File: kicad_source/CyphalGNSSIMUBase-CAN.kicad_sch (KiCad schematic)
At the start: 47 parts, among them CN1 RASPBERRYPI_PICO, CN12 S3B-PH-SM4-TB, CN2 SM04B-SRSS-TB, CN3 SM04B-SRSS-TB, CN7 DNI, CN8 DNI, SW1 PTS636 SM43 SMTR LFS, U3 M24C64-RMN6TP

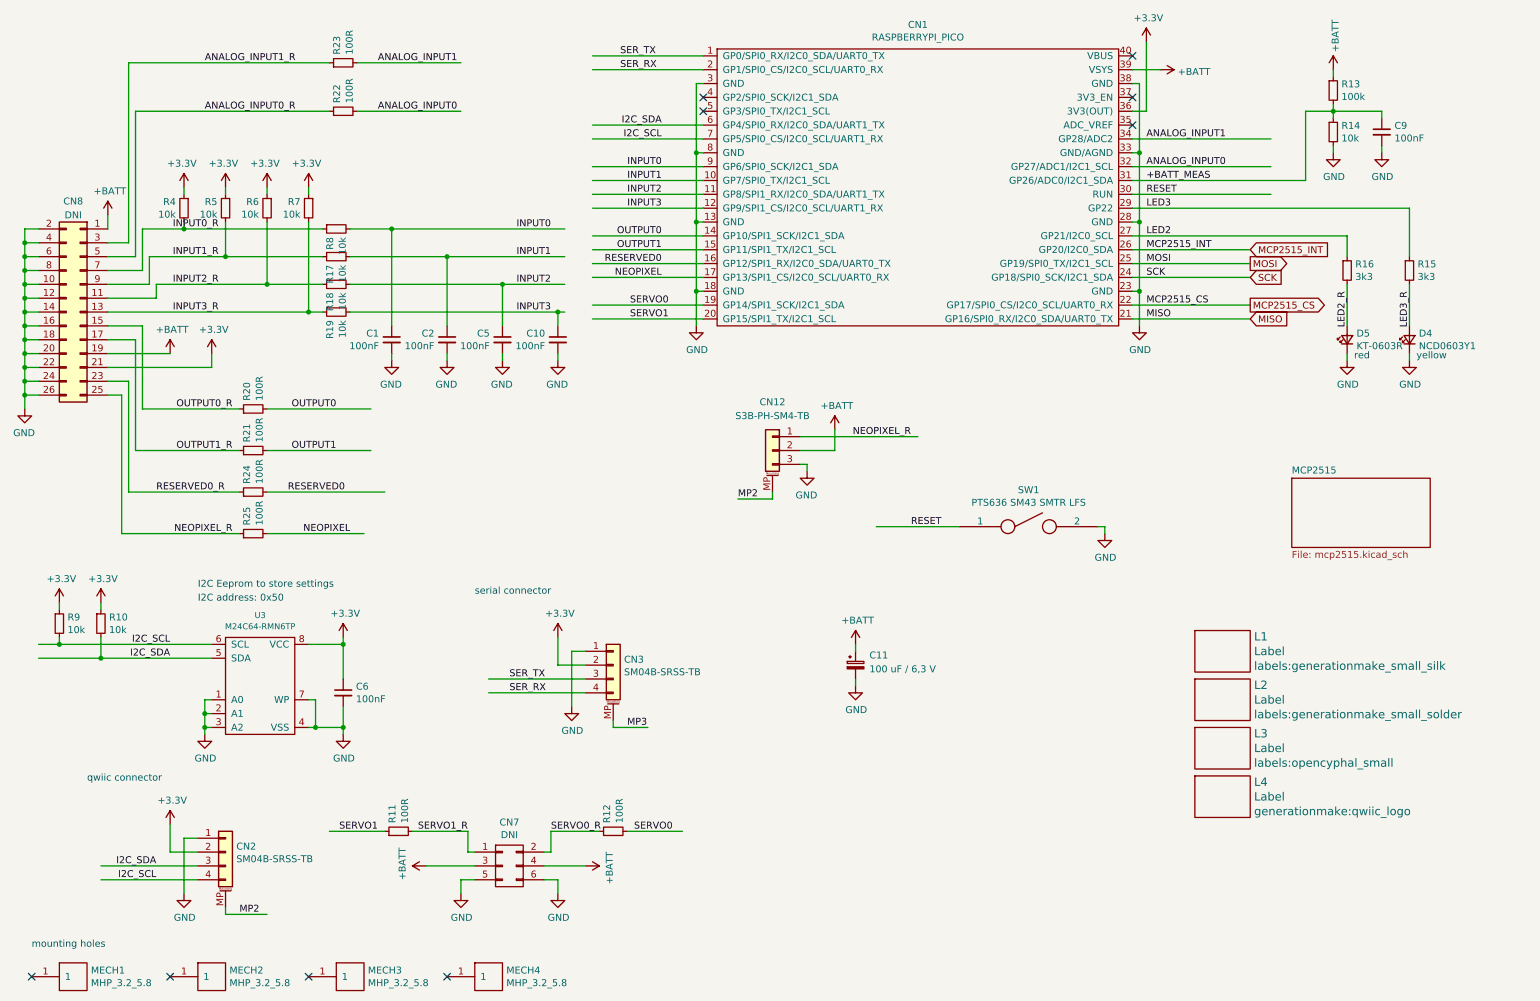
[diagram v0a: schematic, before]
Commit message: removed unnecessary parts
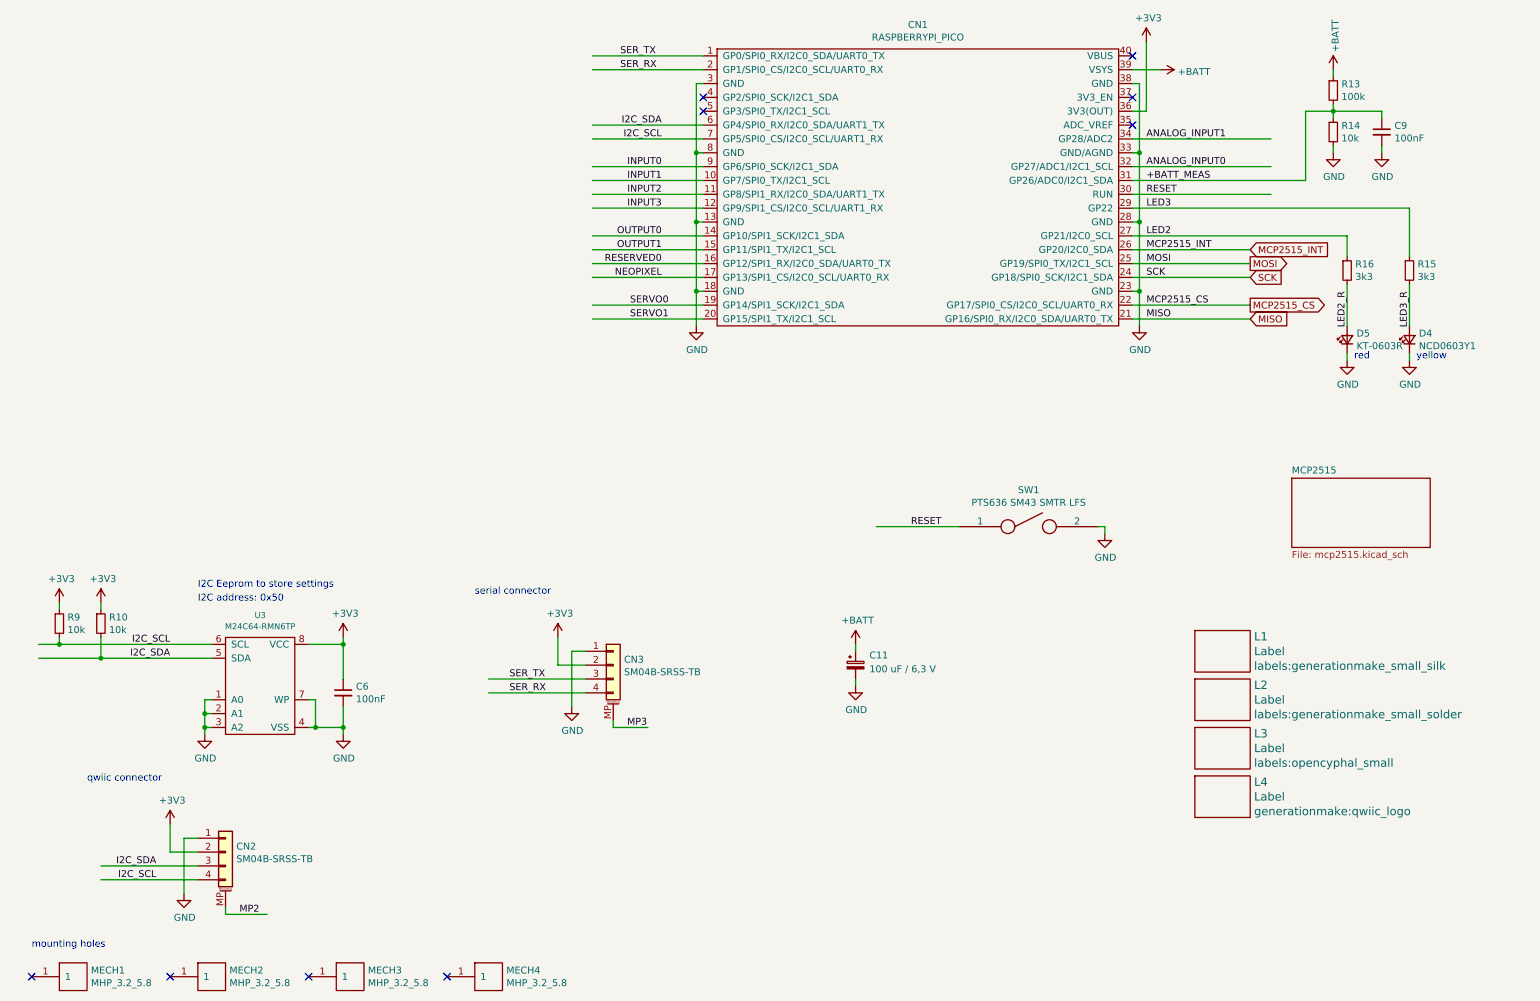
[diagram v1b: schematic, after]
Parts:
- removed C1, C10, C2, C5: 100nF, Capacitor_SMD:C_0603_1608Metric, symbol Device:C_Small
- removed CN12: S3B-PH-SM4-TB, generationmake:JST_PH_S3B-PH-SM4-TB_1x03-1MP_P2.00mm_Horizontal, symbol Connector_Generic_MountingPin:Conn_01x03_MountingPin
- removed CN7: DNI, Connector_PinHeader_2.54mm:PinHeader_2x03_P2.54mm_Horizontal, symbol OpenCyphalPicoBase-rescue:CONN_02X03-mechanical-connectors
- removed CN8: DNI, Connector_PinHeader_2.54mm:PinHeader_2x13_P2.54mm_Vertical, symbol Connector_Generic:Conn_02x13_Odd_Even
- removed R11, R12, R20, R21, R22, R23, R24, R25: 100R, Resistor_SMD:R_0603_1608Metric, symbol Device:R_Small
- removed R17, R18, R19, R4, R5, R6, R7, R8: 10k, Resistor_SMD:R_0603_1608Metric, symbol Device:R_Small
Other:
- title: CyphalPicoBase/CAN -> CyphalGNSSIMUBase/CAN
